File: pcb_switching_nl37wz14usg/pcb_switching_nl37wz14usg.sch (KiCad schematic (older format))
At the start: 8 parts

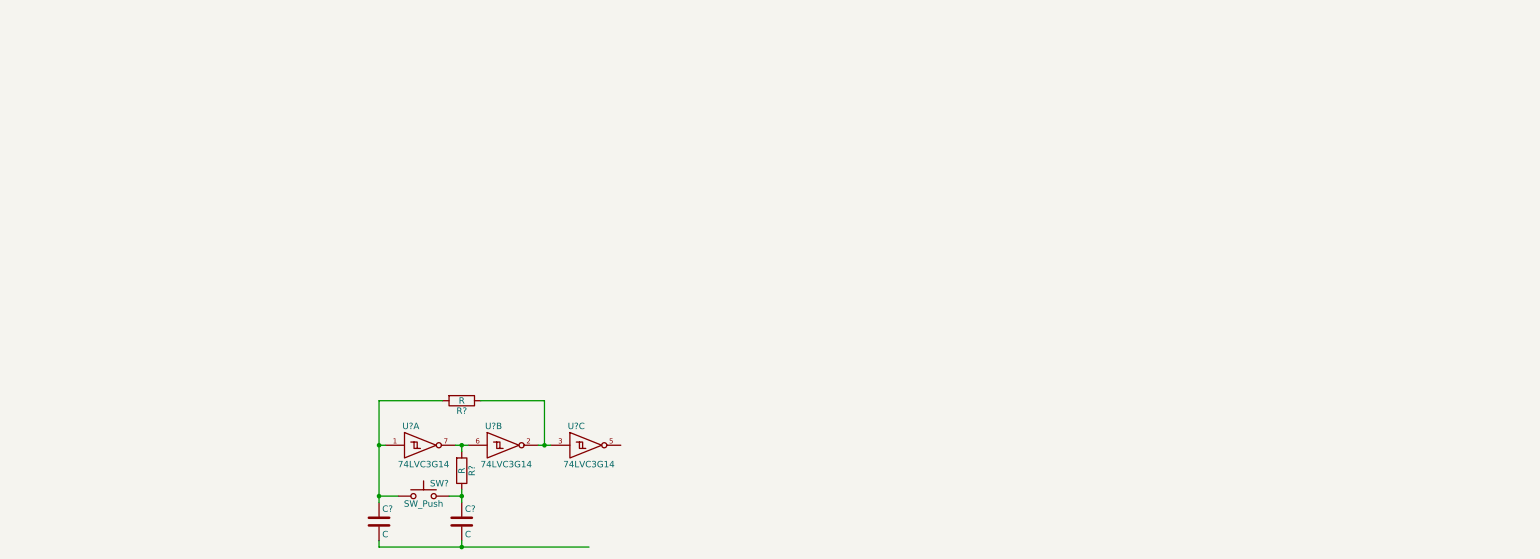
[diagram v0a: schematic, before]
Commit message: Added designer notes for bistable
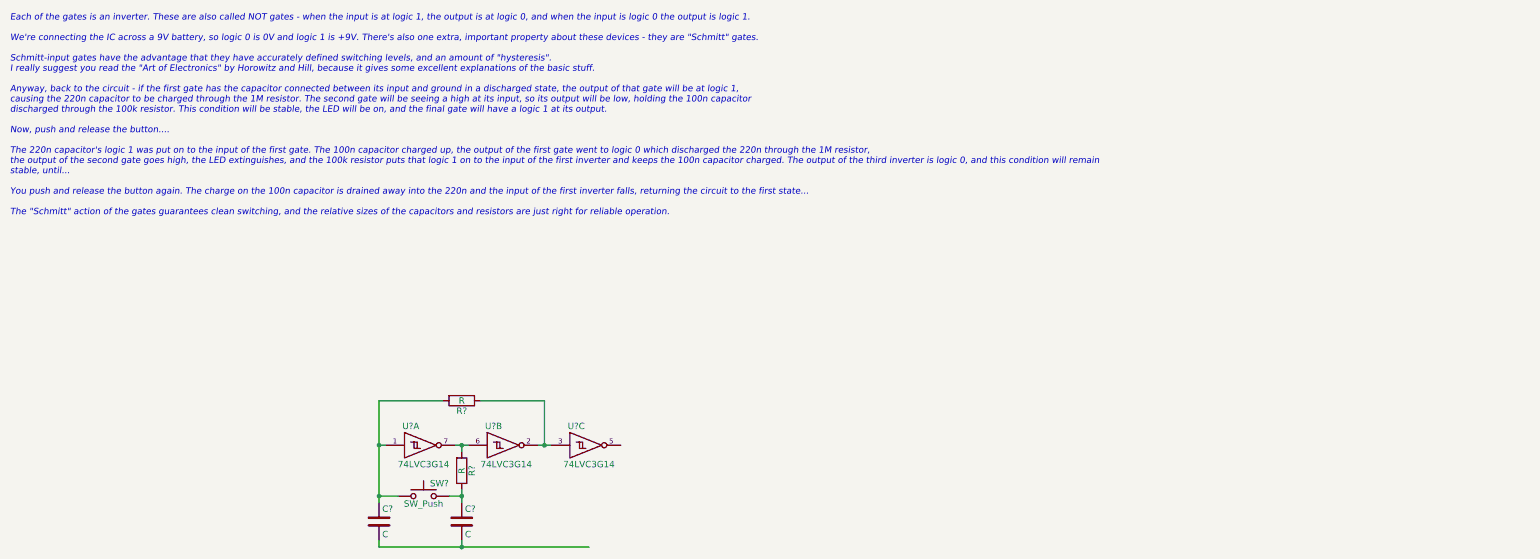
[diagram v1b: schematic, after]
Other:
- note added: "Each of the gates is an inverter. These are also called NOT gates - when the input is at logic 1, the output is at logic 0, and when the input is logic 0 the output is logic 1.\n\nWe're connecting the IC across a 9V battery, so logic 0 is 0V and logic 1 is +9V. There's also one extra, important property about these devices - they are "Schmitt" gates. \n\nSchmitt-input gates have the advantage tha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"
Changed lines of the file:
@@
 	4300 4700 5300 4700
 Connection ~ 4300 4700
+Text Notes 750  2100 0    50   Italic 0
+Each of the gates is an inverter. These are also called NOT gates - when the input is at logic 1, the output is at logic 0, and when the input is logic 0 the output is logic 1.\n\nWe're connecting the IC across a 9V battery, so logic 0 is 0V and logic 1 is +9V. There's also one extra, important property about these devices - they are "Schmitt" gates. \n\nSchmitt-input gates have the advantage that they have accurately defined switching levels, and an amount of "hysteresis". \nI really suggest you read the "Art of Electronics" by Horowitz and Hill, because it gives some excellent explanations of the basic stuff.\n\nAnyway, back to the circuit - if the first gate has the capacitor connected between its input and ground in a discharged state, the output of that gate will be at logic 1, \ncausing the 220n capacitor to be charged through the 1M resistor. The second gate will be seeing a high at its input, so its output will be low, holding the 100n capacitor\ndischarged through the 100k resistor. This condition will be stable, the LED will be on, and the final gate will have a logic 1 at its output.\n\nNow, push and release the button....\n\nThe 220n capacitor's logic 1 was put on to the input of the first gate. The 100n capacitor charged up, the output of the first gate went to logic 0 which discharged the 220n through the 1M resistor,\nthe output of the second gate goes high, the LED extinguishes, and the 100k resistor puts that logic 1 on to the input of the first inverter and keeps the 100n capacitor charged. The output of the third inverter is logic 0, and this condition will remain\nstable, until...\n\nYou push and release the button again. The charge on the 100n capacitor is drained away into the 220n and the input of the first inverter falls, returning the circuit to the first state...\n\nThe "Schmitt" action of the gates guarantees clean switching, and the relative sizes of the capacitors and resistors are just right for reliable operation.
 $EndSCHEMATC

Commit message: detox
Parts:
- C1: renamed from C?; value C -> 100n; footprint (none) -> Capacitor_SMD:C_0603_1608Metric
- C2: renamed from C?; value C -> 220n; footprint (none) -> Capacitor_SMD:C_0603_1608Metric
- R1: renamed from R?; value R -> 100k; footprint (none) -> Capacitor_SMD:C_0603_1608Metric
- R2: renamed from R?; value R -> 1M; footprint (none) -> Capacitor_SMD:C_0603_1608Metric
- SW1: renamed from SW?; footprint (none) -> Connector_Wire:SolderWirePad_1x02_P3.81mm_Drill1mm
- U2: renamed from U?; footprint (none) -> SA_Logic:SN74LVC3G14DCTR
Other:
- note added: "LED cathode connects here"
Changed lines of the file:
@@
 EESchema Schematic File Version 4
+LIBS:pcb_switching_nl37wz14usg-cache
 EELAYER 29 0
 EELAYER END
@@
 $EndDescr
 $Comp
-L 74xGxx:74LVC3G14 U?
+L 74xGxx:74LVC3G14 U2
 U 1 1 5C05FD99
 P 4000 3900
-F 0 "U?" H 3900 4050 50  0000 C CNN
+F 0 "U2" H 3900 4050 50  0000 C CNN
 F 1 "74LVC3G14" H 4000 3750 50  0000 C CNN
-F 2 "" H 4000 3900 50  0001 C CNN
+F 2 "SA_Logic:SN74LVC3G14DCTR" H 4000 3900 50  0001 C CNN
 F 3 "http://www.ti.com/lit/sg/scyt129e/scyt129e.pdf" H 4000 3900 50  0001 C CNN
 	1    4000 3900
@@
 $EndComp
 $Comp
-L 74xGxx:74LVC3G14 U?
+L 74xGxx:74LVC3G14 U2
 U 2 1 5C060470
 P 4650 3900
-F 0 "U?" H 4550 4050 50  0000 C CNN
+F 0 "U2" H 4550 4050 50  0000 C CNN
 F 1 "74LVC3G14" H 4650 3750 50  0000 C CNN
-F 2 "" H 4650 3900 50  0001 C CNN
+F 2 "SA_Logic:SN74LVC3G14DCTR" H 4650 3900 50  0001 C CNN
 F 3 "http://www.ti.com/lit/sg/scyt129e/scyt129e.pdf" H 4650 3900 50  0001 C CNN
 	2    4650 3900
@@
 $EndComp
 $Comp
-L 74xGxx:74LVC3G14 U?
+L 74xGxx:74LVC3G14 U2
 U 3 1 5C06070B
 P 5300 3900
-F 0 "U?" H 5200 4050 50  0000 C CNN
+F 0 "U2" H 5200 4050 50  0000 C CNN
 F 1 "74LVC3G14" H 5300 3750 50  0000 C CNN
-F 2 "" H 5300 3900 50  0001 C CNN
+F 2 "SA_Logic:SN74LVC3G14DCTR" H 5300 3900 50  0001 C CNN
 F 3 "http://www.ti.com/lit/sg/scyt129e/scyt129e.pdf" H 5300 3900 50  0001 C CNN
 	3    5300 3900
@@
 $EndComp
 $Comp
-L Switch:SW_Push SW?
+L Switch:SW_Push SW1
 U 1 1 5C0614D8
 P 4000 4300
-F 0 "SW?" H 4050 4400 50  0000 L CNN
+F 0 "SW1" H 4050 4400 50  0000 L CNN
 F 1 "SW_Push" H 4000 4240 50  0000 C CNN
-F 2 "" H 4000 4500 50  0001 C CNN
+F 2 "Connector_Wire:SolderWirePad_1x02_P3.81mm_Drill1mm" H 4000 4500 50  0001 C CNN
 F 3 "" H 4000 4500 50  0001 C CNN
 	1    4000 4300
@@
 $EndComp
 $Comp
-L Device:R R?
+L Device:R R1
 U 1 1 5C0636BC
 P 4300 3550
-F 0 "R?" V 4380 3550 50  0000 C CNN
-F 1 "R" V 4300 3550 50  0000 C CNN
-F 2 "" V 4230 3550 50  0001 C CNN
+F 0 "R1" V 4380 3550 50  0000 C CNN
+F 1 "100k" V 4300 3550 50  0000 C CNN
+F 2 "Capacitor_SMD:C_0603_1608Metric" V 4230 3550 50  0001 C CNN
 F 3 "~" H 4300 3550 50  0001 C CNN
 	1    4300 3550
@@
 $EndComp
 $Comp
-L Device:R R?
+L Device:R R2
 U 1 1 5C0639A1
 P 4300 4100
-F 0 "R?" V 4380 4100 50  0000 C CNN
-F 1 "R" V 4300 4100 50  0000 C CNN
-F 2 "" V 4230 4100 50  0001 C CNN
+F 0 "R2" V 4380 4100 50  0000 C CNN
+F 1 "1M" V 4300 4100 50  0000 C CNN
+F 2 "Capacitor_SMD:C_0603_1608Metric" V 4230 4100 50  0001 C CNN
 F 3 "~" H 4300 4100 50  0001 C CNN
 	1    4300 4100
@@
 $EndComp
 $Comp
-L Device:C C?
+L Device:C C1
 U 1 1 5C063FA4
 P 3650 4500
-F 0 "C?" H 3675 4600 50  0000 L CNN
-F 1 "C" H 3675 4400 50  0000 L CNN
-F 2 "" H 3688 4350 50  0001 C CNN
+F 0 "C1" H 3675 4600 50  0000 L CNN
+F 1 "100n" H 3675 4400 50  0000 L CNN
+F 2 "Capacitor_SMD:C_0603_1608Metric" H 3688 4350 50  0001 C CNN
 F 3 "~" H 3650 4500 50  0001 C CNN
 	1    3650 4500
@@
 $EndComp
 $Comp
-L Device:C C?
+L Device:C C2
 U 1 1 5C06438A
 P 4300 4500
-F 0 "C?" H 4325 4600 50  0000 L CNN
-F 1 "C" H 4325 4400 50  0000 L CNN
-F 2 "" H 4338 4350 50  0001 C CNN
+F 0 "C2" H 4325 4600 50  0000 L CNN
+F 1 "220n" H 4325 4400 50  0000 L CNN
+F 2 "Capacitor_SMD:C_0603_1608Metric" H 4338 4350 50  0001 C CNN
 F 3 "~" H 4300 4500 50  0001 C CNN
 	1    4300 4500
@@
 Text Notes 750  2100 0    50   Italic 0
 Each of the gates is an inverter. These are also called NOT gates - when the input is at logic 1, the output is at logic 0, and when the input is logic 0 the output is logic 1.\n\nWe're connecting the IC across a 9V battery, so logic 0 is 0V and logic 1 is +9V. There's also one extra, important property about these devices - they are "Schmitt" gates. \n\nSchmitt-input gates have the advantage that they have accurately defined switching levels, and an amount of "hysteresis". \nI really suggest you read the "Art of Electronics" by Horowitz and Hill, because it gives some excellent explanations of the basic stuff.\n\nAnyway, back to the circuit - if the first gate has the capacitor connected between its input and ground in a discharged state, the output of that gate will be at logic 1, \ncausing the 220n capacitor to be charged through the 1M resistor. The second gate will be seeing a high at its input, so its output will be low, holding the 100n capacitor\ndischarged through the 100k resistor. This condition will be stable, the LED will be on, and the final gate will have a logic 1 at its output.\n\nNow, push and release the button....\n\nThe 220n capacitor's logic 1 was put on to the input of the first gate. The 100n capacitor charged up, the output of the first gate went to logic 0 which discharged the 220n through the 1M resistor,\nthe output of the second gate goes high, the LED extinguishes, and the 100k resistor puts that logic 1 on to the input of the first inverter and keeps the 100n capacitor charged. The output of the third inverter is logic 0, and this condition will remain\nstable, until...\n\nYou push and release the button again. The charge on the 100n capacitor is drained away into the 220n and the input of the first inverter falls, returning the circuit to the first state...\n\nThe "Schmitt" action of the gates guarantees clean switching, and the relative sizes of the capacitors and resistors are just right for reliable operation.
+Wire Notes Line
+	4950 3900 4950 4400
+Wire Notes Line
+	4950 4400 5250 4400
+Text Notes 4950 4400 0    50   ~ 0
+LED cathode connects here
 $EndSCHEMATC
